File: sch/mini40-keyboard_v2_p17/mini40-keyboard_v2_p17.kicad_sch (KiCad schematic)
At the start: 17 parts, among them J1 Conn_01x02, Q1 DMG2301L, U1 Pico

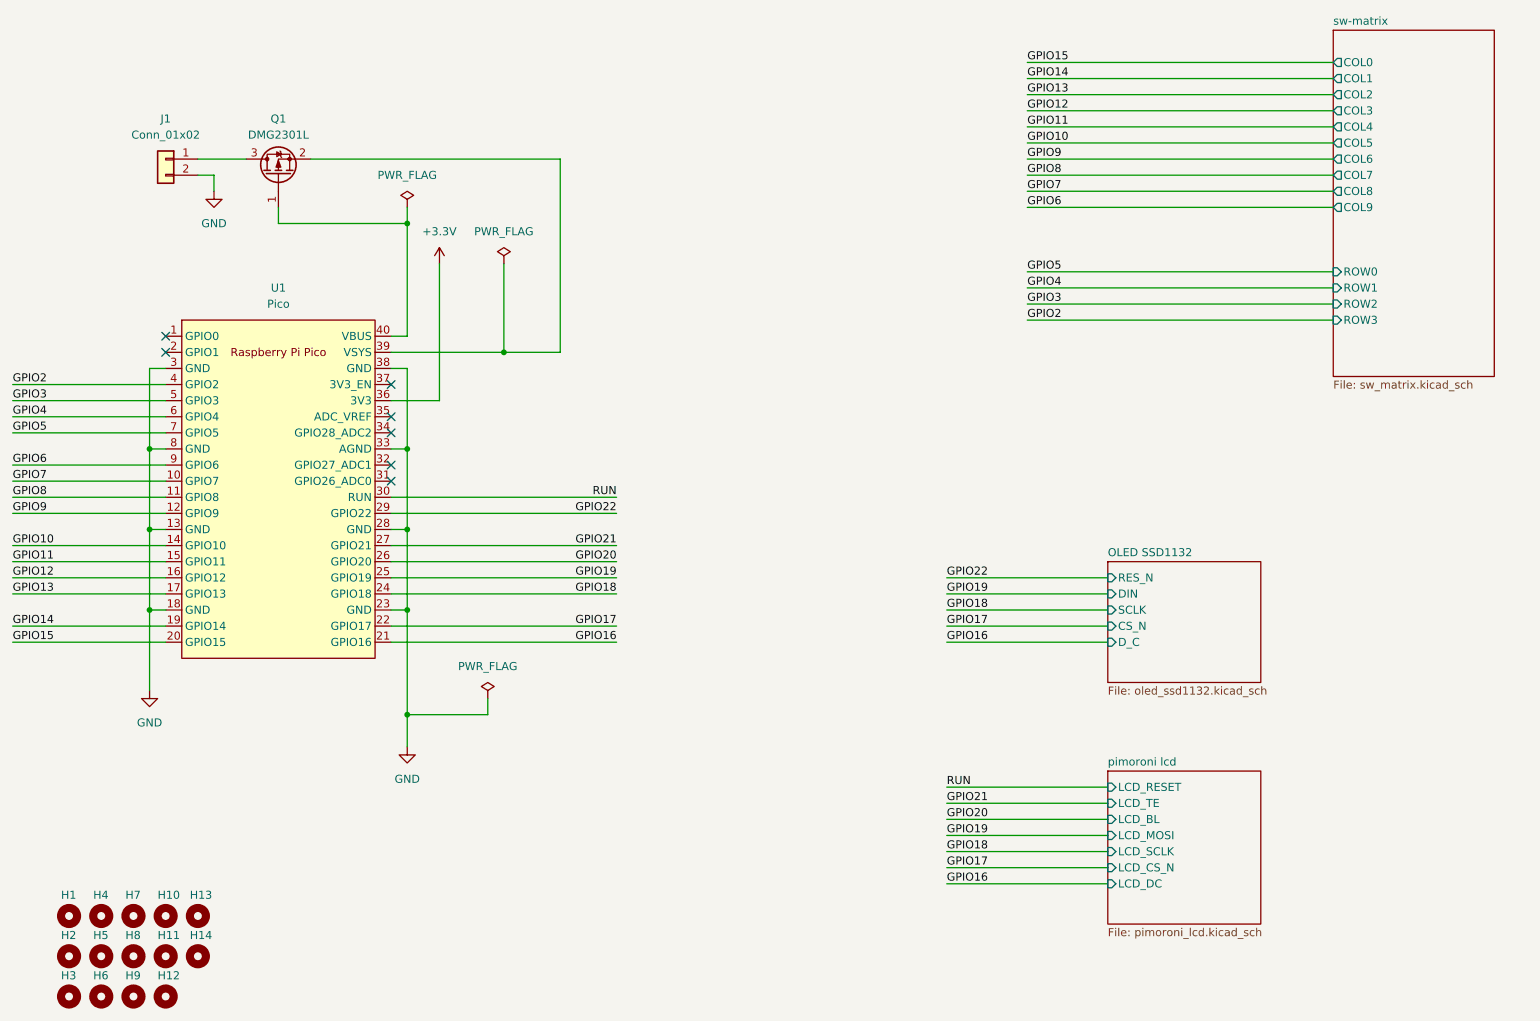
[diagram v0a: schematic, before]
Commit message: マイコンとしてESP32-S3の使用を検討しています。 Rasberry Pi Pico と ESP32-S3 のどちらかを選択して実装する設計です。 主要部品以外は仮の部品・フットプリントです。
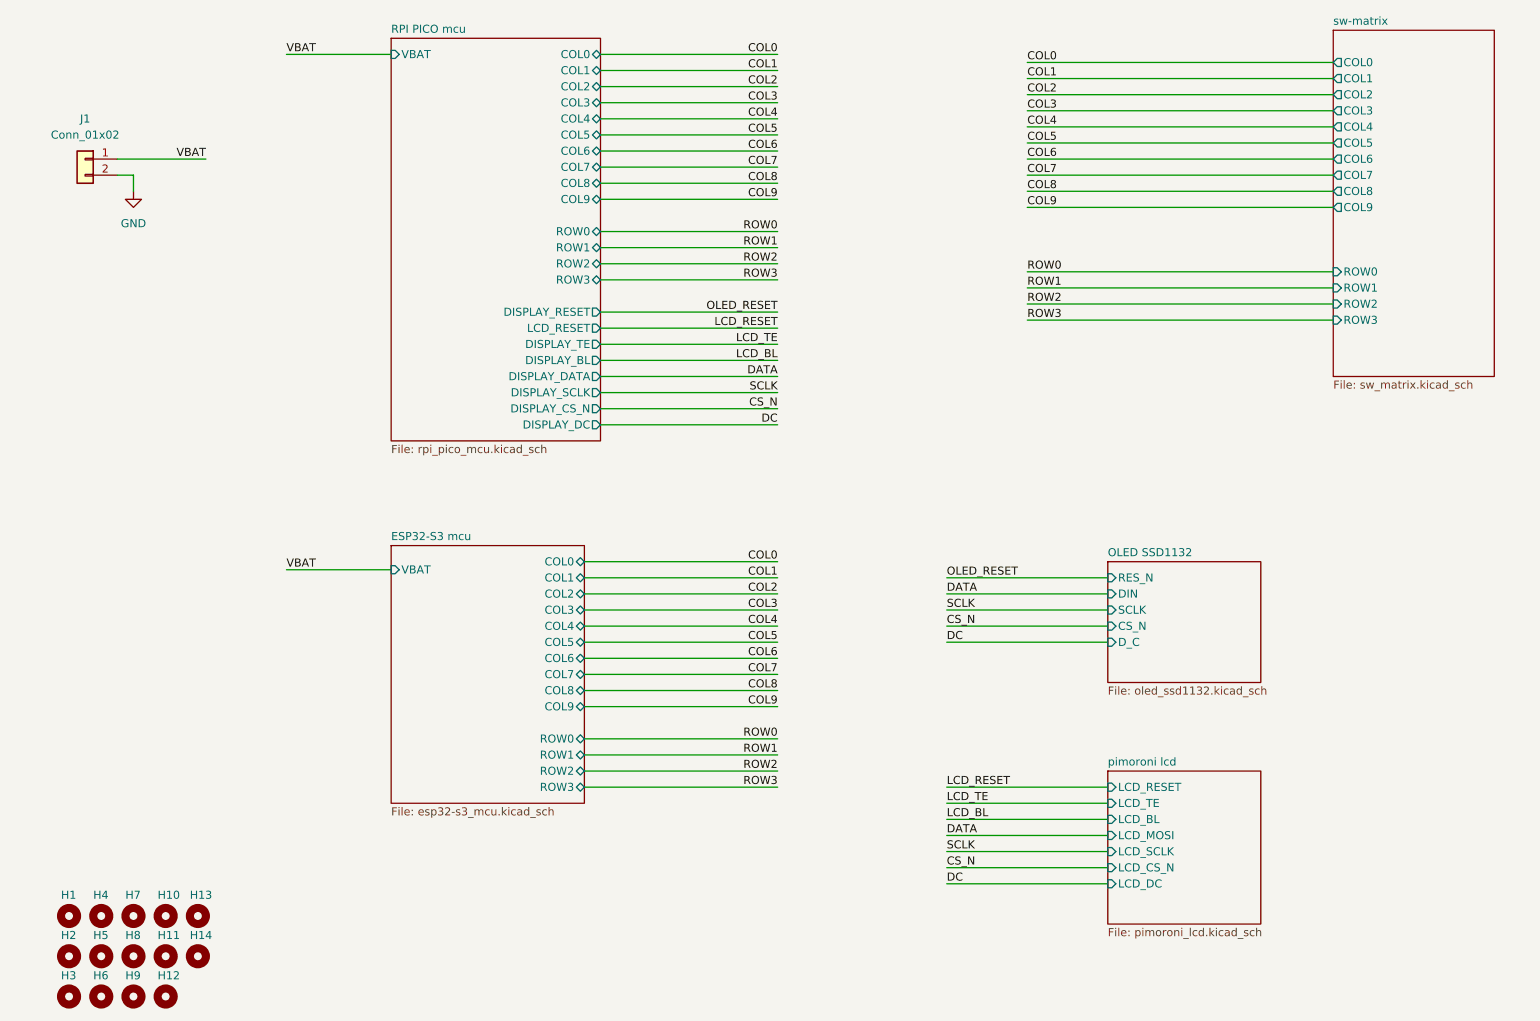
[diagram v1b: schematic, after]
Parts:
- removed Q1: DMG2301L, Package_TO_SOT_SMD:SOT-23, symbol Transistor_FET:DMG2301L
- removed U1: Pico, my_pico:pico_no_dbg_smd_th_p0.85, symbol my_pico:my_pico_no_dbg
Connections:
- net VBAT: now reaches J1.1 (Pin_1)
- no-connect marks 7 -> 0
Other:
- added sheet ESP32-S3 mcu (esp32-s3_mcu.kicad_sch)
- added sheet RPI PICO mcu (rpi_pico_mcu.kicad_sch)
- moved on the sheet: J1
